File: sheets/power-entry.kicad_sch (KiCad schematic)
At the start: 0 parts

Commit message: Schematic capture: power entry (p2) and regulators (p3)
Pages 2 and 3 drawn to the schematic rules adopted on 2026-10-22 (wired
clusters in dashed boxes, labels only between clusters and sheets, one
rail symbol per cluster, every net named, D-45 values with separate
voltage/tolerance/dielectric fields). Design values and their reasons
are on each sheet. Parts not yet in the DropOut library are stock
Device symbols marked PLACEHOLDER with empty MPN fields.

The root index now carries the sheet interfaces as sheet pins, laid out
along the power and signal path. check_schematic.py also fails on
auto-generated net names (rule O-2). CLAUDE.md records the four project
answers and the net-naming decisions.

Co-Authored-By: Claude Opus 5.5 <noreply@anthropic.com>
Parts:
- added C (x7): 100nF, symbol Device:C
- added C: 47uF, symbol Device:C_Polarized
- added C: 68nF, symbol Device:C
- added C: 470nF, symbol Device:C
- added C (x4): 10nF, symbol Device:C
- added C (x2): 4.7uF, symbol Device:C
- added D: XLD8A24CAHM3_A_I, DropOut_Diode_SMD:D_DO-218AC, symbol DropOut_Protection:XLD8A24CAHM3_A_I
- added L: TBD, symbol Device:L
- added Q (x4): NMOS, symbol Device:Q_NMOS
- added R: 7.87k, symbol Device:R
- added R (x3): 10k, symbol Device:R
- added R: 49.9R, symbol Device:R
- added R: 32k, symbol Device:R
- added R: 2k, symbol Device:R
- added R: 0R, symbol Device:R
- added R: 107k, symbol Device:R
- added R: 10R, symbol Device:R
- added R: 250uR, symbol Device:R_Shunt
- added R: 2.1k, symbol Device:R
- added TH: 10k, symbol Device:Thermistor_NTC
- added TP: TP_GND, symbol Connector:TestPoint
- added TP: TP_BATT_MON, symbol Connector:TestPoint
- added TP: TP_RSENSE_N, symbol Connector:TestPoint
- added TP: TP_VBAT_PROT, symbol Connector:TestPoint
- added TP: TP_LM_FLT_L, symbol Connector:TestPoint
- added TP: TP_VBAT_D, symbol Connector:TestPoint
- added TP: TP_INH, symbol Connector:TestPoint
- added TP: TP_RSENSE_P, symbol Connector:TestPoint
- added TP: TP_VBAT_FILT, symbol Connector:TestPoint
- added TP: TP_VBAT_IN, symbol Connector:TestPoint
- added U: LM74910HQRGERQ1, DropOut_Package_DFN_QFN:Texas_RGE0024T_VQFN-24-1EP_4x4mm_P0.5mm_EP2.1x2.1mm, symbol DropOut_Power:LM74910HQRGERQ1
- added U: INA228AQDGSRQ1, DropOut_Package_SO:Texas_DGS0010A_TSSOP-10_3x3mm_P0.5mm, symbol DropOut_Sensor:INA228AQDGSRQ1
- added U: TMP175AQDGKRQ1, DropOut_Package_SO:Texas_DGK0008A_TSSOP-8_3x3mm_P0.65mm, symbol DropOut_Sensor:TMP175AQDGKRQ1
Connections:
- new net 3V3_MAIN: C.1, C.1, R.1, R.1, R.1, U.6 (VS), U.8 (V+)
- new net BATT_MON: C.1, R.1, R.2, TP.1
- new net DGATE: Q.G, Q.G, U.1 (DGATE)
- new net GND: C.2, C.2, C.2, C.2, C.2, C.2, C.2, C.2, C.2, C.2, C.2, C.2, C.2, D.1 (A1), R.2, R.2, TH.2, TP.1, U.1 (A1), U.13 (GND), U.2 (A0), U.4 (GND), U.5 (A2), U.6 (A1), U.7 (A0), U.7 (GND)
- new net HGATE: R.2, U.14 (HGATE)
- new net HGATE_G: C.1, Q.G, Q.G, R.1
- new net I2C0_TELEMETRY_SCL: U.2 (SCL), U.5 (SCL)
- new net I2C0_TELEMETRY_SDA: U.1 (SDA), U.4 (SDA)
- new net INH: TP.1, U.7 (~{SLEEP})
- new net LM_CAP: C.2, U.23 (CAP)
- new net LM_CSP: C.2, R.2, U.20 (CS+)
- new net LM_FLT_L: R.2, TP.1, U.12 (~{FLT})
- new net LM_ILIM: R.1, U.11 (ILIM)
- new net LM_ISCP: C.1, R.2, U.18 (ISCP)
- new net LM_OV: R.1, R.2, U.5 (OV)
- new net LM_SW: R.1, U.3 (SW)
- new net LM_TMR: C.1, U.9 (TMR)
- new net LM_UVLO: R.1, R.2, U.4 (UVLO)
- new net NTC_RSENSE: C.1, R.2, TH.1
- new net RSENSE_N: C.1, C.2, R.3, TP.1, U.19 (CS-), U.9 (IN-)
- new net RSENSE_P: R.1, R.1, R.2, TP.1, U.10 (IN+)
- new net TMP175_ALERT_L: R.2, U.3 (ALERT)
- new net VBAT_D: C.1, C.1, Q.D, Q.D, R.1, TP.1, U.22 (VS), U.24 (C), U.6 (EN)
- new net VBAT_FILT: C.1, C.1, L.2, TP.1
- new net VBAT_IN: C.1, D.2 (A2), Q.S, Q.S, TP.1, U.2 (A)
- new net VBAT_PROT: C.1, C.1, C.1, L.1, Q.S, Q.S, TP.1, U.15 (OUT), U.16 (SLEEP_OV), U.8 (VBUS)
- new net VBAT_Q2D: Q.D, Q.D, R.4
- no-connect marks 0 -> 6
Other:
- note added: "60 A path: TVS, ideal-diode FETs, shared RSENSE, disconnect FETs (D201, Q201-Q204, R201)"
- note added: "DESIGN VALUES (LM74910H-Q1 SNOSDE6C sec. 9.2; Node60 DEC-001). Values per DropOut D-45. R(ILIM) = 12 x RSET / (RSENSE x ILIM) = 12 x 49.9 / (0.25m x 32k) = 74.9 A breaker (Rev A: 75 A). RSET 49.9R: E96 value nearest the 50R in Rev A (50-100R allowed). R(ILIM) 32k: E192, 1 %. Fast SCP: ISCP to RSENSE_P through R204 0R (no RISCP shift) -> 20 mV default = 80 A. R204 keeps the RISCP option (VSNS_SCP 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"
- note added: "EMI filter, regulator branch: VBAT_PROT to VBAT_FILT (L201)"
- note added: "FET-bank temperature, I2C 0x48 (U203)"
- note added: "Ideal-diode / OCP controller with OV, UV and BATT_MON ladder (U201)"
- note added: "LM74910H sense inputs (R203, R204, C211, C212)"
- note added: "Power flags (ERC)"
- note added: "RSENSE temperature: NTC divider (R209, TH201, C215)"
- note added: "Test points"
- note added: "Total-current monitor, I2C 0x40 (U202)"
- title: Node60 -> Node60 · A · Power entry (p2)

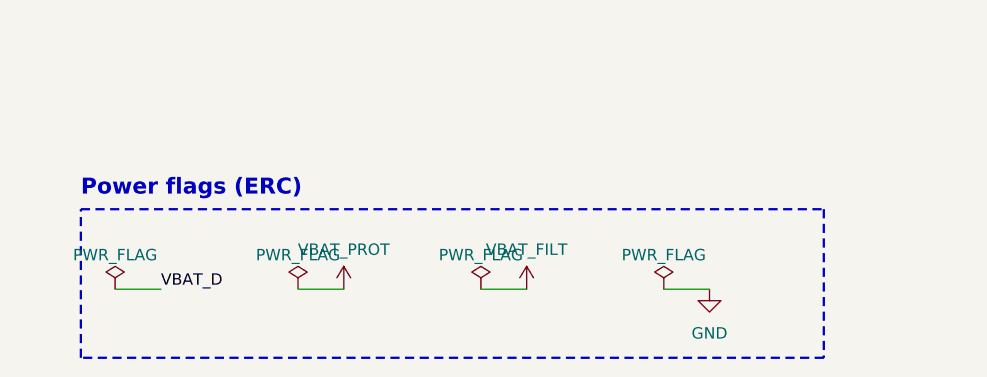
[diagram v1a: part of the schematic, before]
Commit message: Schematic capture: MCU and NVM (p4), connectors (p9); ERC clean
Page 4: S32K344 in eight boxed units. The supply unit has decoupling per
NXP HDG Rev E2 Table 2; each port unit shows its pin plan and firmware
notes (D-14 as adopted). Pins were checked against NXP's IOMUX table:
EMAC RMII per NXP's TJA1100 use case, LPSPI4 switch chain, LPSPI2 log
flash, LPI2C0 telemetry, ADC1/ADC2 inputs, EIRQ fault lines, SWD and an
LPUART0 debug port. Also the IS25LP032D flash, the Cortex 10-pin header
and the I2C pull-ups.

Page 9: placeholder battery, return, T1S and MX150 output connectors
(all TBD selections), mirrored with pin 1 at the top (D-43), and the
PWR_FLAGs for nets entering the board.

ERC: 0 violations. 17 items are excluded in node60.kicad_pro, each with
its reason (D-52): parallel output pins typed power output in the
library (to be retyped there), and two LAN8670 pins tied to VSS per the
datasheet.

Co-Authored-By: Claude Opus 5.5 <noreply@anthropic.com>
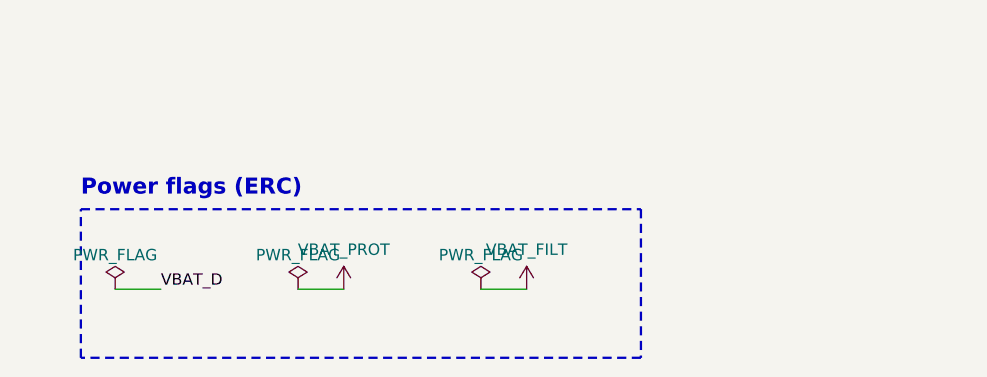
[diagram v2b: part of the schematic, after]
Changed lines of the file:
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@@
 	(rectangle
 		(start 26.67 334.01)
-		(end 109.22 350.52)
+		(end 88.9 350.52)
 		(stroke
 			(width 0.254)
@@
 					(unit 1)
 				)
-			)
-		)
-	)
-	(symbol
-		(lib_id "power:PWR_FLAG")
-		(at 91.44 342.9 0)
-		(unit 1)
-		(body_style 1)
-		(exclude_from_sim no)
-		(in_bom yes)
-		(on_board yes)
-		(in_pos_files yes)
-		(dnp no)
-		(property "Reference" "#FLG040"
-			(at 91.44 342.9 0)
-			(effects
-				(font
-					(size 1.27 1.27)
-				)
-				(hide yes)
-			)
-		)
-		(property "Value" "PWR_FLAG"
-			(at 91.44 339.1 0)
-			(effects
-				(font
-					(size 1.27 1.27)
-				)
-			)
-		)
-		(property "Footprint" ""
-			(at 91.44 342.9 0)
-			(effects
-				(font
-					(size 1.27 1.27)
-				)
-				(hide yes)
-			)
-		)
-		(property "Datasheet" ""
-			(at 91.44 342.9 0)
-			(effects
-				(font
-					(size 1.27 1.27)
-				)
-				(hide yes)
-			)
-		)
-		(pin "1"
-		)
-		(instances
-			(project "node60"
-				(path "/55f51841-30a3-4965-b848-b796f60054d0/822dbac5-68ee-4519-a5d1-8bcf1992c5d9"
-					(reference "#FLG02040")
-					(unit 1)
-				)
-			)
-		)
-	)
-	(wire
-		(pts
-			(xy 91.44 342.9)
-			(xy 96.52 342.9)
-		)
-		(stroke
-			(width 0)
-			(type default)
-		)
-	)
-	(symbol
-		(lib_id "power:GND")
-		(at 96.52 342.9 0)
-		(unit 1)
-		(body_style 1)
-		(exclude_from_sim no)
-		(in_bom yes)
-		(on_board yes)
-		(in_pos_files yes)
-		(dnp no)
-		(property "Reference" "#PWR041"
-			(at 96.52 342.9 0)
-			(effects
-				(font
-					(size 1.27 1.27)
-				)
-				(hide yes)
-			)
-		)
-		(property "Value" "GND"
-			(at 96.52 347.8 0)
-			(effects
-				(font
-					(size 1.27 1.27)
-				)
-			)
-		)
-		(property "Footprint" ""
-			(at 96.52 342.9 0)
-			(effects
-				(font
-					(size 1.27 1.27)
-				)
-				(hide yes)
-			)
-		)
-		(property "Datasheet" ""
-			(at 96.52 342.9 0)
-			(effects
-				(font
-					(size 1.27 1.27)
-				)
-				(hide yes)
-			)
-		)
-		(pin "1"
-		)
-		(instances
-			(project "node60"
-				(path "/55f51841-30a3-4965-b848-b796f60054d0/822dbac5-68ee-4519-a5d1-8bcf1992c5d9"
-					(reference "#PWR02041")
-					(unit 1)
-				)

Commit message: Record TBD part selections; schematic follows them
User selections of 2026-10-22: TPS7B8133QWDRVRQ1 (VDDAU LDO),
CSS2725FTL250 (0.25 mOhm RSENSE), IAUTN08S5N012LATMA1 (DGATE/HGATE
FETs, new parts entry) and NCU18XH103F6SRB (NTCs), each with its dated
DigiKey observation and the rejected or alternative candidates, which
are now parts entries too. The schematic placeholders carry the
selected MPNs until the library parts land. CCAP grows to 1uF:
10 x the summed Ciss of four IAUTN08S5N012L is 0.61 uF.

Co-Authored-By: Claude Opus 5.5 <noreply@anthropic.com>
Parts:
- C: value 470nF -> 1uF; Package 0603 -> 0805
- Q: value NMOS -> IAUTN08S5N012L; Placeholder PLACEHOLDER: TBD part: selection pending user decision (fin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 -> PLACEHOLDER: selected 2026-10-22: Infineon IAUTN08S5N012LAT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
- R: value 250uR -> CSS2725FTL250; Placeholder PLACEHOLDER: TBD part: selection pending user decision (fin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 -> PLACEHOLDER: selected 2026-10-22: Stackpole CSS2725FTL250; 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
- TH: value 10k -> NCU18XH103F6SRB; Placeholder PLACEHOLDER: TBD part: selection pending user decision (fin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 -> PLACEHOLDER: selected 2026-10-22: Murata NCU18XH103F6SRB; l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
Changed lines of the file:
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@@
 			)
 		)
-		(property "Value" "NMOS"
+		(property "Value" "IAUTN08S5N012L"
 			(at 97.155 77.47 0)
 			(effects
@@
 			)
 		)
-		(property "Placeholder" "PLACEHOLDER: TBD part: selection pending user decision (find-part), then a library session (DGATE/HGATE MOSFETs, 80-100 V AEC-Q101)"
+		(property "Placeholder" "PLACEHOLDER: selected 2026-10-22: Infineon IAUTN08S5N012LATMA1; library part pending (session node60-fets-shunts)"
 			(at 91.44 76.2 0)
 			(effects
@@
 			)
 		)
-		(property "Value" "NMOS"
+		(property "Value" "IAUTN08S5N012L"
 			(at 120.015 77.47 0)
 			(effects
@@
 			)
 		)
-		(property "Placeholder" "PLACEHOLDER: TBD part: selection pending user decision (find-part), then a library session (DGATE/HGATE MOSFETs, 80-100 V AEC-Q101)"
+		(property "Placeholder" "PLACEHOLDER: selected 2026-10-22: Infineon IAUTN08S5N012LATMA1; library part pending (session node60-fets-shunts)"
 			(at 114.3 76.2 0)
 			(effects
@@
 			)
 		)
-		(property "Value" "250uR"
+		(property "Value" "CSS2725FTL250"
 			(at 137.16 68.716 90)
 			(effects
@@
 			)
 		)
-		(property "Placeholder" "PLACEHOLDER: TBD part: selection pending user decision (find-part), then a library session (TBD-RSENSE-0R25: 0.25 mOhm 1 % AEC-Q200, >= 1.5 W)"
+		(property "Placeholder" "PLACEHOLDER: selected 2026-10-22: Stackpole CSS2725FTL250; library part pending (session node60-fets-shunts)"
 			(at 137.16 63.5 0)
 			(effects
@@
 			)
 		)
-		(property "Value" "NMOS"
+		(property "Value" "IAUTN08S5N012L"
 			(at 173.355 77.47 0)
 			(effects
@@
 			)
 		)
-		(property "Placeholder" "PLACEHOLDER: TBD part: selection pending user decision (find-part), then a library session (DGATE/HGATE MOSFETs, 80-100 V AEC-Q101)"
+		(property "Placeholder" "PLACEHOLDER: selected 2026-10-22: Infineon IAUTN08S5N012LATMA1; library part pending (session node60-fets-shunts)"
 			(at 167.64 76.2 0)
 			(effects
@@
 			)
 		)
-		(property "Value" "NMOS"
+		(property "Value" "IAUTN08S5N012L"
 			(at 196.215 77.47 0)
 			(effects
@@
 			)
 		)
-		(property "Placeholder" "PLACEHOLDER: TBD part: selection pending user decision (find-part), then a library session (DGATE/HGATE MOSFETs, 80-100 V AEC-Q101)"
+		(property "Placeholder" "PLACEHOLDER: selected 2026-10-22: Infineon IAUTN08S5N012LATMA1; library part pending (session node60-fets-shunts)"
 			(at 190.5 76.2 0)
 			(effects
@@
 			)
 		)
-		(property "Value" "470nF"
+		(property "Value" "1uF"
 			(at 226.822 170.18 0)
 			(effects
@@
 			)
 		)
-		(property "Package" "0603"
+		(property "Package" "0805"
 			(at 223.52 168.91 0)
 			(effects
@@
 			)
 		)
-		(property "Value" "10k"
+		(property "Value" "NCU18XH103F6SRB"
 			(at 479.298 203.2 0)
 			(effects
@@
 			)
 		)
-		(property "Placeholder" "PLACEHOLDER: TBD part: selection pending user decision (find-part), then a library session (TBD-NTC-10K: 0603, R25 1 %, B 1 %, AEC-Q200)"
+		(property "Placeholder" "PLACEHOLDER: selected 2026-10-22: Murata NCU18XH103F6SRB; library part pending (session node60-ldo-ntc)"
 			(at 476.25 201.93 0)
 			(effects
@@
 		)
 	)
-	(text "DESIGN VALUES (LM74910H-Q1 SNOSDE6C sec. 9.2; Node60 DEC-001). Values per DropOut D-45.\nR(ILIM) = 12 x RSET / (RSENSE x ILIM) = 12 x 49.9 / (0.25m x 32k) = 74.9 A breaker (Rev A: 75 A).\n  RSET 49.9R: E96 value nearest the 50R in Rev A (50-100R allowed). R(ILIM) 32k: E192, 1 %.\nFast SCP: ISCP to RSENSE_P through R204 0R (no RISCP shift) -> 20 mV default = 80 A.\n  R204 keeps the RISCP option (VSNS_SCP = 10.5 uA x RISCP + 20 mV); C212 is the DNP deglitch option (D-48).\nCTMR 68nF C0G: T(OC) = 1.2 x 68n / 82.3u = 0.99 ms; retry = 22.7e6 x 68n = 1.5 s. Tune vs inrush (GATE-PWR-01).\nCCAP 470nF 50V: >= 10 x sum(Ciss) of Q201-Q204; re-check when the FETs are chosen. CVS 100nF 100V.\nRG 10R + Cdvdt 10nF on HGATE: inrush slew = 55 uA / 10 nF = 5.5 V/ms.\nOV/UV/BATT_MON ladder, 118.97k total (< 120k leakage rule), 1 %:\n  OV rising = 0.60 V x 118.97k / 2.1k  = 34.0 V   (disconnects above 34 V; passes 24 V jump start)\n  UVLO fall = 0.55 V x 118.97k / 11.97k = 5.47 V  (rising 0.60 V -> 5.96 V)\n  BATT_MON = SW x 9.97k / 118.97k = SW / 11.93 (1:12 concept); 3.3 V full scale = 39.4 V\n  BATT_MON source 9.1 k with 10nF C0G (tau 91 us): set the ADC sample time from this.\n  The SW switch opens in SLEEP, so the ladder draws nothing while parked.\nEN tied to VS (always on). SLEEP = INH: parked = SLEEP mode (6 uA; OUT fed by the 7R bypass, 100 mA peak).\nSLEEP_OV = OUT: overvoltage CLAMP mode while parked (~21 V), so VDDAU stays up through a jump start.\nIMON floating (INA228 fitted). RTN pad floating per datasheet. FLT 10k pull-up to 3V3_MAIN (low when off).\nINA228 A1 = A0 = GND -> 0x40; ALERT unused. ADCRANGE = 1 (+/-40.96 mV); SHUNT_CAL in firmware.\nTMP175 A2..A0 = GND -> 0x48. Place beside the FET bank. NTC tight to the RSENSE body (GATE-TMP-01).\nNTC_RSENSE: 10k 0.1 % over NTC, ratiometric to VREFH = 3V3_MAIN; 5 k source, 100nF C0G (tau 0.5 ms).\nRSENSE Kelvin: two separate star pairs from the sense pads, one to U201 (via R203/R204), one to U202.\nCapacitors on battery nets are 100 V (>= 2x the 34 V OV cut-off, derating rule).\nMOSFETs: 2 + 2 drawn as placeholders; count and part follow the surge/thermal calculation (DEC-001).\nEMI filter on the regulator branch only; L201 and C208 TBD (finalize after emissions test).\nUNVERIFIED (release-blocking): FET count/part, RSENSE part, EMI filter values, parked leakage of U202 inputs.\n"
+	(text "DESIGN VALUES (LM74910H-Q1 SNOSDE6C sec. 9.2; Node60 DEC-001). Values per DropOut D-45.\nR(ILIM) = 12 x RSET / (RSENSE x ILIM) = 12 x 49.9 / (0.25m x 32k) = 74.9 A breaker (Rev A: 75 A).\n  RSET 49.9R: E96 value nearest the 50R in Rev A (50-100R allowed). R(ILIM) 32k: E192, 1 %.\nFast SCP: ISCP to RSENSE_P through R204 0R (no RISCP shift) -> 20 mV default = 80 A.\n  R204 keeps the RISCP option (VSNS_SCP = 10.5 uA x RISCP + 20 mV); C212 is the DNP deglitch option (D-48).\nCTMR 68nF C0G: T(OC) = 1.2 x 68n / 82.3u = 0.99 ms; retry = 22.7e6 x 68n = 1.5 s. Tune vs inrush (GATE-PWR-01).\nCCAP 1uF 50V: >= 10 x sum(Ciss) = 10 x 4 x 15.3 nF = 0.61 uF for 4 x IAUTN08S5N012L. CVS 100nF 100V.\nRG 10R + Cdvdt 10nF on HGATE: inrush slew = 55 uA / 10 nF = 5.5 V/ms.\nOV/UV/BATT_MON ladder, 118.97k total (< 120k leakage rule), 1 %:\n  OV rising = 0.60 V x 118.97k / 2.1k  = 34.0 V   (disconnects above 34 V; passes 24 V jump start)\n  UVLO fall = 0.55 V x 118.97k / 11.97k = 5.47 V  (rising 0.60 V -> 5.96 V)\n  BATT_MON = SW x 9.97k / 118.97k = SW / 11.93 (1:12 concept); 3.3 V full scale = 39.4 V\n  BATT_MON source 9.1 k with 10nF C0G (tau 91 us): set the ADC sample time from this.\n  The SW switch opens in SLEEP, so the ladder draws nothing while parked.\nEN tied to VS (always on). SLEEP = INH: parked = SLEEP mode (6 uA; OUT fed by the 7R bypass, 100 mA peak).\nSLEEP_OV = OUT: overvoltage CLAMP mode while parked (~21 V), so VDDAU stays up through a jump start.\nIMON floating (INA228 fitted). RTN pad floating per datasheet. FLT 10k pull-up to 3V3_MAIN (low when off).\nINA228 A1 = A0 = GND -> 0x40; ALERT unused. ADCRANGE = 1 (+/-40.96 mV); SHUNT_CAL in firmware.\nTMP175 A2..A0 = GND -> 0x48. Place beside the FET bank. NTC tight to the RSENSE body (GATE-TMP-01).\nNTC_RSENSE: 10k 0.1 % over NTC, ratiometric to VREFH = 3V3_MAIN; 5 k source, 100nF C0G (tau 0.5 ms).\nRSENSE Kelvin: two separate star pairs from the sense pads, one to U201 (via R203/R204), one to U202.\nCapacitors on battery nets are 100 V (>= 2x the 34 V OV cut-off, derating rule).\nMOSFETs: IAUTN08S5N012L (80 V, 1.15 mOhm), 2 per bank: ~0.6 mOhm, ~2 W per bank at 60 A. Confirm with the\n  surge/thermal calculation (DEC-001). RSENSE CSS2725FTL250: 0.9 W at 60 A, 4 W rated.\nEMI filter on the regulator branch only; L201 and C208 TBD (finalize after emissions test).\nUNVERIFIED (release-blocking): FET count (thermal), EMI filter values, parked leakage of U202 inputs.\n"
 		(exclude_from_sim no)
 		(at 358.14 266.7 0)

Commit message: Swap placeholders for merged DropOut library parts
Library bumped to ce98ecf (PRs #15, #16, #18, #19, #20, #21 merged).
Now real parts: IAUTN08S5N012LATMA1 (Q201-Q204, dual gate: G_ON and
G_LIN both driven), CSS2725FTL250 (R201, 2-terminal: sense nets are
VBAT_D / VBAT_Q2D with Kelvin taps from the pads in layout),
TPS7B8133QWDRVRQ1 (U301, COUT 2.2uF per its 1-200 uF requirement),
NCU18XH103F6SRB (RT201, RT601-801), Wurth 74438356022HT / 74438356010HT
buck inductors and Harwin S1751-46R GND loops (user's picks 2026-10-23),
1 mm pad test points and DT13-2P output headers. The library pin-type
fixes cut the ERC exclusions from 17 to 2. parts.yaml records the
library symbols; the library tables list the new libraries.

Co-Authored-By: Claude Opus 5.5 <noreply@anthropic.com>
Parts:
- removed TH: NCU18XH103F6SRB, symbol Device:Thermistor_NTC
- removed TP: TP_GND, symbol Connector:TestPoint
- added RT: NCU18XH103F6SRB, DropOut_Resistor_SMD:R_NTC_0603_1608Metric_Pad0.7x0.7mm, symbol DropOut_Thermistor:NCU18XH103F6SRB
- Q: value IAUTN08S5N012L -> IAUTN08S5N012LATMA1; footprint (none) -> DropOut_Package_TO_SOT_SMD:Infineon_PG-HSOF-8-2; symbol Device:Q_NMOS -> DropOut_PowerSwitch:IAUTN08S5N012LATMA1; DigiKey_PN (none) -> 448-IAUTN08S5N012LATMA1CT-ND; MPN (none) -> IAUTN08S5N012LATMA1; Manufacturer (none) -> Infineon Technologies; Mouser_PN (none) -> 726-IAUTN08S5N012LAT; Notes (none) -> Dual gate: G_ON (pin 1) and G_LIN (pin 2) must both be driv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; Placeholder PLACEHOLDER: selected 2026-10-22: Infineon IAUTN08S5N012LAT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 -> (none); Temperature_Grade (none) -> AEC-Q101, Tj -55 to +175 °C
- R: footprint (none) -> DropOut_Resistor_SMD:R_Shunt_Stackpole_CSS2725; symbol Device:R_Shunt -> DropOut_Resistor:CSS2725FTL250; DigiKey_PN (none) -> CSS2725FTL250CT-ND; MPN (none) -> CSS2725FTL250; Manufacturer (none) -> Stackpole Electronics; Mouser_PN (none) -> 708-CSS2725FTL250; Placeholder PLACEHOLDER: selected 2026-10-22: Stackpole CSS2725FTL250; 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 -> (none); Temperature_Grade (none) -> AEC-Q200, -55 to +225 °C; Tolerance 1% -> (none)
- TP: value TP_BATT_MON -> TP_LM_FLT_L
- TP: value TP_RSENSE_N -> TP_BATT_MON
- TP: value TP_VBAT_PROT -> TP_VBAT_Q2D
- TP: value TP_LM_FLT_L -> TP_INH
- TP: value TP_INH -> TP_GND; Type 1mm pad -> probe loop
- TP: value TP_RSENSE_P -> TP_VBAT_FILT
- TP: value TP_VBAT_FILT -> TP_VBAT_PROT
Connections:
- net BATT_MON: now also TP.1; no longer TP.1
- net DGATE: now also Q.1 (G_ON), Q.1 (G_ON), Q.2 (G_LIN), Q.2 (G_LIN); no longer Q.G, Q.G
- net GND: now also TP.1, RT.2
- net HGATE_G: now also Q.1 (G_ON), Q.1 (G_ON), Q.2 (G_LIN), Q.2 (G_LIN); no longer Q.G, Q.G
- net INH: now also TP.1; no longer TP.1
- net LM_FLT_L: now also TP.1; no longer TP.1
- net NTC_RSENSE: now also RT.1
- net VBAT_D: now also Q.9 (D), Q.9 (D), R.1, R.1, U.10 (IN+); no longer Q.D, Q.D
- net VBAT_FILT: now also TP.1; no longer TP.1
- net VBAT_IN: now also Q.3 (S), Q.3 (S), Q.4 (S), Q.4 (S), Q.5 (S), Q.5 (S), Q.6 (S), Q.6 (S), Q.7 (S), Q.7 (S), Q.8 (S), Q.8 (S); no longer Q.S, Q.S
- net VBAT_PROT: now also Q.3 (S), Q.3 (S), Q.4 (S), Q.4 (S), Q.5 (S), Q.5 (S), Q.6 (S), Q.6 (S), Q.7 (S), Q.7 (S), Q.8 (S), Q.8 (S), TP.1; no longer Q.S, Q.S, TP.1
- net VBAT_Q2D: now also C.1, C.2, Q.9 (D), Q.9 (D), R.2, TP.1, U.19 (CS-), U.9 (IN-); no longer Q.D, Q.D, R.4
- removed net RSENSE_N: C.1, C.2, R.3, TP.1, U.19 (CS-), U.9 (IN-)
- removed net RSENSE_P: R.1, R.1, R.2, TP.1, U.10 (IN+)
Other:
- note added: "DESIGN VALUES (LM74910H-Q1 SNOSDE6C sec. 9.2; Node60 DEC-001). Values per DropOut D-45. R(ILIM) = 12 x RSET / (RSENSE x ILIM) = 12 x 49.9 / (0.25m x 32k) = 74.9 A breaker (Rev A: 75 A). RSET 49.9R: E96 value nearest the 50R in Rev A (50-100R allowed). R(ILIM) 32k: E192, 1 %. Fast SCP: ISCP to the R201 VBAT_D pad through R204 0R (no RISCP shift) -> 20 mV default = 80 A. R204 keeps the RISCP option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"
- note added: "RSENSE temperature: NTC divider (R2xx, RT201, C2xx)"
- note removed: "DESIGN VALUES (LM74910H-Q1 SNOSDE6C sec. 9.2; Node60 DEC-001). Values per DropOut D-45. R(ILIM) = 12 x RSET / (RSENSE x ILIM) = 12 x 49.9 / (0.25m x 32k) = 74.9 A breaker (Rev A: 75 A). RSET 49.9R: E96 value nearest the 50R in Rev A (50-100R allowed). R(ILIM) 32k: E192, 1 %. Fast SCP: ISCP to RSENSE_P through R204 0R (no RISCP shift) -> 20 mV default = 80 A. R204 keeps the RISCP option (VSNS_SCP 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"
- note removed: "RSENSE temperature: NTC divider (R209, TH201, C215)"
- moved on the sheet: C, L, R
